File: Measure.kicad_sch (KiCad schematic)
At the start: 34 parts, among them J1 Input, J2 Output, J3 +5V, U1 TMR_1-0511

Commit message: Первая версия в производство
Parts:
- added H1, H2, H3, H4: MountingHole, MountingHole:MountingHole_3.2mm_M3, symbol Mechanical:MountingHole
- C13, C2: value C_Small -> 1u
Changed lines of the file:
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@@
     (pin "2")
+  )
+  (symbol (lib_id "Mechanical:MountingHole") (at 74.168 130.048 0) (unit 1)
+    (in_bom yes) (on_board yes) (fields_autoplaced)
+    (property "Reference" "H1" (id 0) (at 77.47 128.7779 0)
+      (effects (font (size 1.27 1.27)) (justify left))
+    )
+    (property "Value" "MountingHole" (id 1) (at 77.47 131.3179 0)
+      (effects (font (size 1.27 1.27)) (justify left))
+    )
+    (property "Footprint" "MountingHole:MountingHole_3.2mm_M3" (id 2) (at 74.168 130.048 0)
+      (effects (font (size 1.27 1.27)) hide)
+    )
+    (property "Datasheet" "~" (id 3) (at 74.168 130.048 0)
+      (effects (font (size 1.27 1.27)) hide)
+    )
   )
   (symbol (lib_id "power:GNDPWR") (at 59.944 63.754 0) (unit 1)
@@
       (effects (font (size 1.27 1.27)) (justify left))
     )
-    (property "Value" "C_Small" (id 1) (at 161.671 62.6172 0)
+    (property "Value" "1u" (id 1) (at 161.671 62.6172 0)
       (effects (font (size 1.27 1.27)) (justify left))
     )
@@
     (pin "1")
     (pin "2")
+  )
+  (symbol (lib_id "Mechanical:MountingHole") (at 74.676 143.256 0) (unit 1)
+    (in_bom yes) (on_board yes) (fields_autoplaced)
+    (property "Reference" "H3" (id 0) (at 77.978 141.9859 0)
+      (effects (font (size 1.27 1.27)) (justify left))
+    )
+    (property "Value" "MountingHole" (id 1) (at 77.978 144.5259 0)
+      (effects (font (size 1.27 1.27)) (justify left))
+    )
+    (property "Footprint" "MountingHole:MountingHole_3.2mm_M3" (id 2) (at 74.676 143.256 0)
+      (effects (font (size 1.27 1.27)) hide)
+    )
+    (property "Datasheet" "~" (id 3) (at 74.676 143.256 0)
+      (effects (font (size 1.27 1.27)) hide)
+    )
   )
   (symbol (lib_id "Device:C_Small") (at 247.523 60.833 0) (unit 1)
@@
       (effects (font (size 1.27 1.27)) (justify left))
     )
-    (property "Value" "C_Small" (id 1) (at 39.624 62.4902 0)
+    (property "Value" "1u" (id 1) (at 39.624 62.4902 0)
       (effects (font (size 1.27 1.27)) (justify left))
     )
@@
     (pin "1")
     (pin "2")
+  )
+  (symbol (lib_id "Mechanical:MountingHole") (at 74.93 149.86 0) (unit 1)
+    (in_bom yes) (on_board yes) (fields_autoplaced)
+    (property "Reference" "H4" (id 0) (at 78.232 148.5899 0)
+      (effects (font (size 1.27 1.27)) (justify left))
+    )
+    (property "Value" "MountingHole" (id 1) (at 78.232 151.1299 0)
+      (effects (font (size 1.27 1.27)) (justify left))
+    )
+    (property "Footprint" "MountingHole:MountingHole_3.2mm_M3" (id 2) (at 74.93 149.86 0)
+      (effects (font (size 1.27 1.27)) hide)
+    )
+    (property "Datasheet" "~" (id 3) (at 74.93 149.86 0)
+      (effects (font (size 1.27 1.27)) hide)
+    )
   )
   (symbol (lib_id "Device:C_Small") (at 119.126 60.706 0) (unit 1)
@@
     (pin "4")
   )
+  (symbol (lib_id "Mechanical:MountingHole") (at 74.422 136.398 0) (unit 1)
+    (in_bom yes) (on_board yes) (fields_autoplaced)
+    (property "Reference" "H2" (id 0) (at 77.724 135.1279 0)
+      (effects (font (size 1.27 1.27)) (justify left))
+    )
+    (property "Value" "MountingHole" (id 1) (at 77.724 137.6679 0)
+      (effects (font (size 1.27 1.27)) (justify left))
+    )
+    (property "Footprint" "MountingHole:MountingHole_3.2mm_M3" (id 2) (at 74.422 136.398 0)
+      (effects (font (size 1.27 1.27)) hide)
+    )
+    (property "Datasheet" "~" (id 3) (at 74.422 136.398 0)
+      (effects (font (size 1.27 1.27)) hide)
+    )
+  )
   (symbol (lib_id "power:GND") (at 124.714 109.982 0) (unit 1)
     (in_bom yes) (on_board yes)
@@
     )
     (path "/ce0183bd-126a-4a79-9acb-8b4bfe630f86"
-      (reference "C2") (unit 1) (value "C_Small") (footprint "Capacitor_SMD:C_0805_2012Metric_Pad1.18x1.45mm_HandSolder")
+      (reference "C2") (unit 1) (value "1u") (footprint "Capacitor_SMD:C_0805_2012Metric_Pad1.18x1.45mm_HandSolder")
     )
     (path "/21e3bd42-09d5-4909-b490-5b05f0b8e880"
@@
     )
     (path "/2a7ac3c0-b782-4a36-8e14-9fb9fc4b9e99"
-      (reference "C13") (unit 1) (value "C_Small") (footprint "Capacitor_SMD:C_0805_2012Metric_Pad1.18x1.45mm_HandSolder")
+      (reference "C13") (unit 1) (value "1u") (footprint "Capacitor_SMD:C_0805_2012Metric_Pad1.18x1.45mm_HandSolder")
     )
     (path "/7ef98de2-0407-484c-b75f-d3f0938f17b0"
@@
       (reference "D5") (unit 1) (value "HCPL788J") (footprint "Package_SO:SOIC-16W_7.5x10.3mm_P1.27mm")
     )
+    (path "/1bc22e41-50b0-4676-86e9-a264ed264ea5"
+      (reference "H1") (unit 1) (value "MountingHole") (footprint "MountingHole:MountingHole_3.2mm_M3")
+    )
+    (path "/f4077211-e2b9-4e29-b066-b7867371809f"
+      (reference "H2") (unit 1) (value "MountingHole") (footprint "MountingHole:MountingHole_3.2mm_M3")
+    )
+    (path "/2fb6fd09-e0b5-4e7f-bfd7-b71afc6fbc75"
+      (reference "H3") (unit 1) (value "MountingHole") (footprint "MountingHole:MountingHole_3.2mm_M3")
+    )
+    (path "/d4e4fe2a-1928-4bd8-9a9b-ad36c3abd4fd"
+      (reference "H4") (unit 1) (value "MountingHole") (footprint "MountingHole:MountingHole_3.2mm_M3")
+    )
     (path "/b349c6a9-3f69-433c-8ef8-1939e03de70e"

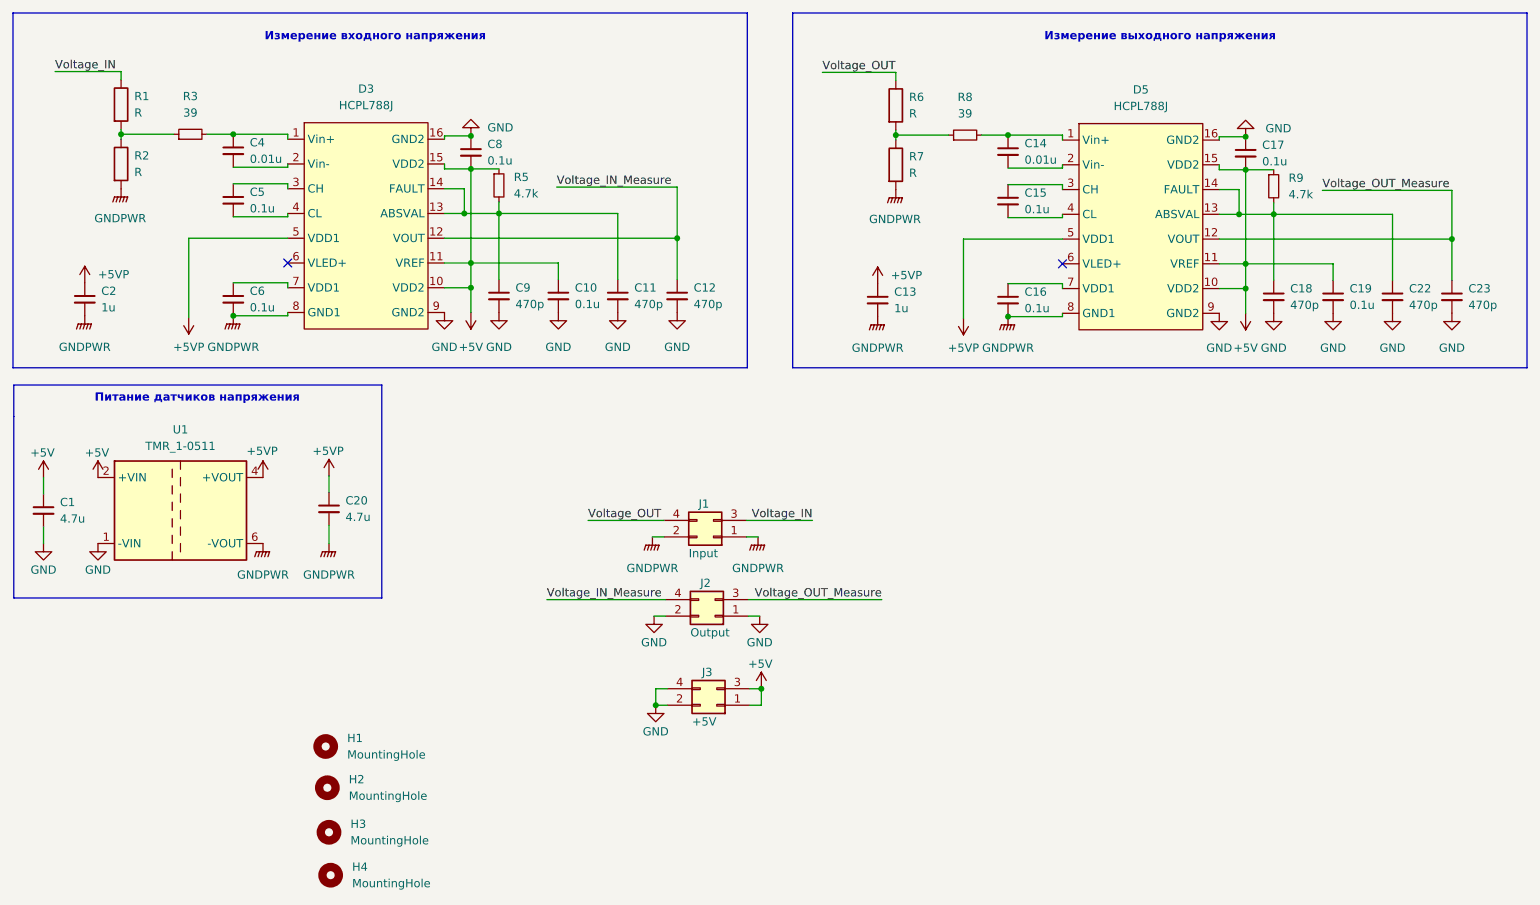
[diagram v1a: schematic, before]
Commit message: Исправлены ошибки с неподключённым IN- и питанием
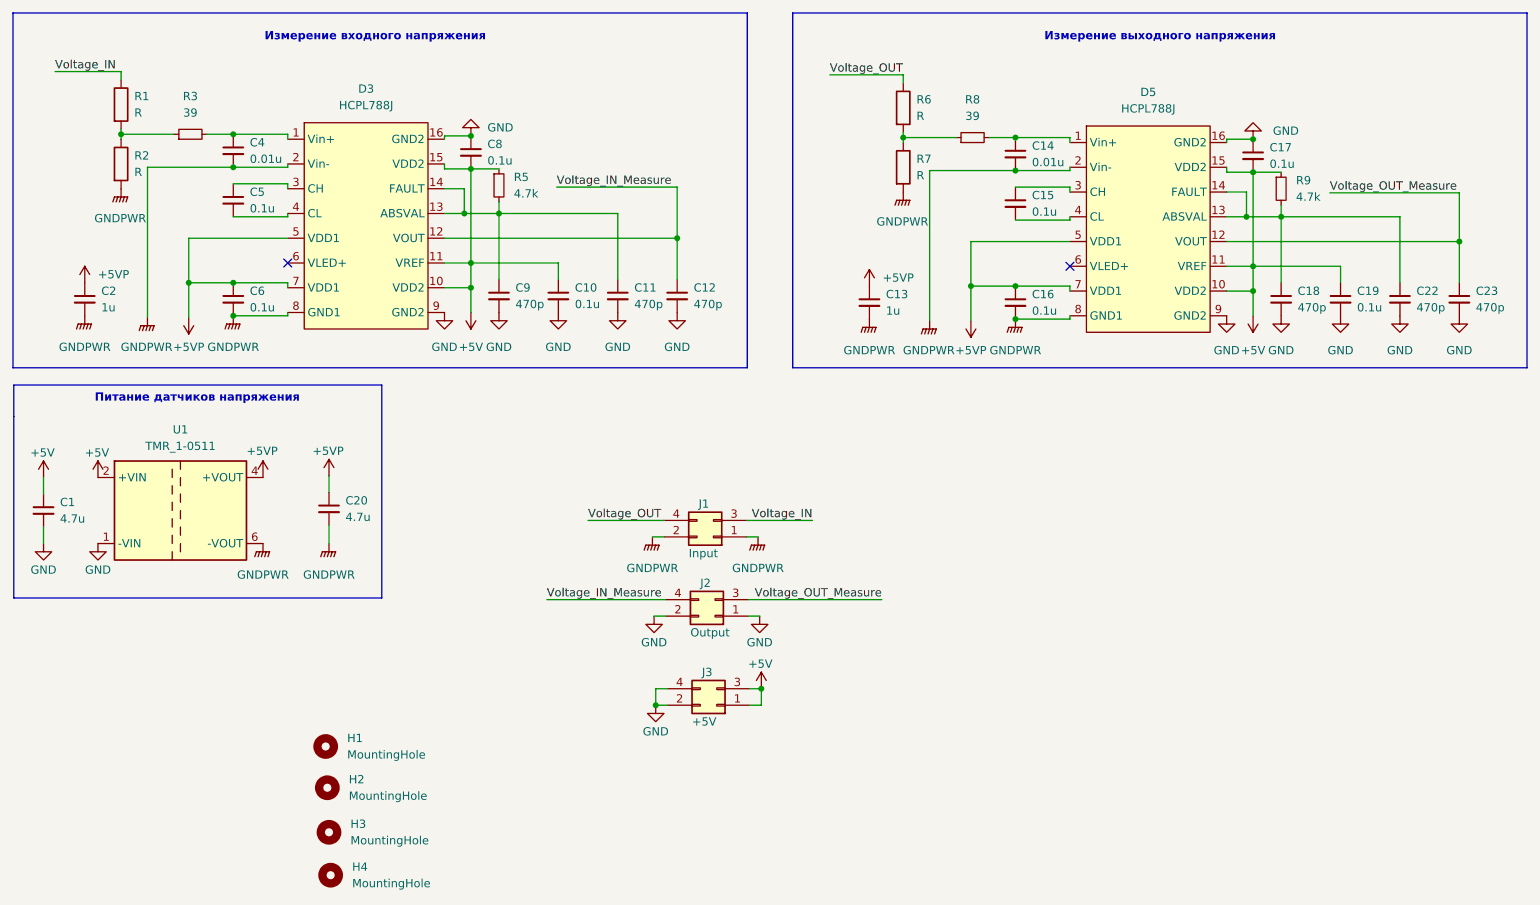
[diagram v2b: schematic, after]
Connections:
- net +5VP: now also C16.1, C6.1, D3.7 (VDD1), D5.7 (VDD1)
- net GNDPWR: now also C14.2, C4.2, D3.2 (Vin-), D5.2 (Vin-)
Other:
- moved on the sheet: C13, C14, C15, C16, C17, C18, C19, C22, C23, D5, R6, R7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
